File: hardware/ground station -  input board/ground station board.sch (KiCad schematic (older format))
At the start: 28 parts, among them J1 Conn_01x08_Female, J10 High_Pwr_Connector(Female), J2 Conn_01x08_Male, J3 Conn_01x08_Female, J4 Conn_01x08_Male, J5 Conn_01x06_Female, J6 Conn_01x06_Male, J7 Conn_01x06_Female, J8 Conn_01x06_Male, J9 Battery_Connector(Male)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

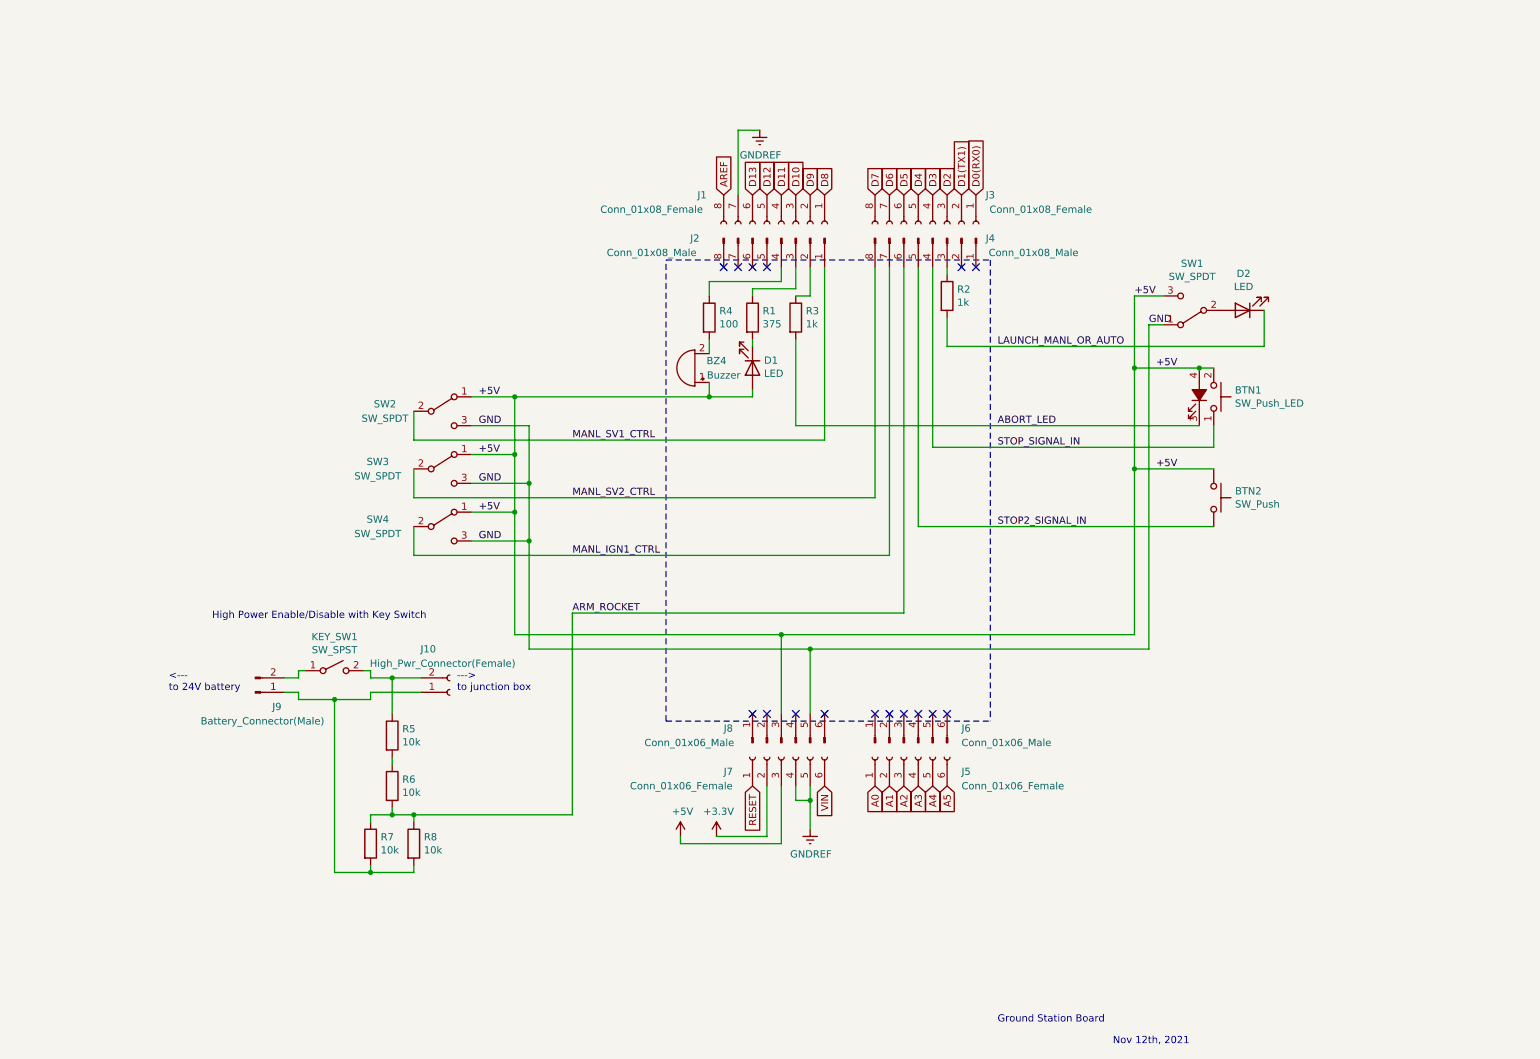
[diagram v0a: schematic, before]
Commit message: Updated Ground Station board, Junction Box sensor board, and Junction Box high power board.
Moved Ground Station pins so that abort (STOP), backup abort (BACKUP_STOP),  auto/manual launch (LAUNCH_MANL_OR_AUTO), and arming (ARM_ROCKET) signals now each go to an Arduino pin that can handle external interrupts. Shifted the rest of the pins so that the manual control pins for SV1, SV2, and IGN1 all connect to the same header on the Arduino. Added battery and outlet for extension cord to key switch circuit. Removed some male header pins because red radio XBee board must connect to them on Arduino instead. As  a consequence, the armed status buzzer/LED pins connect to male headers a level below the board using wires. XBee board also blocks nearest 5V/GND pins, so power must be obtained from the very end of the
Arduino Mega board, using external wires connected to male headers.

Added fuses to high power board. One fuse for each solid state relay, and one fuse from the main 24V high power line.

Corrected wiring for GND, D9, and D8 on sensor board's 4 pin connector (which controls the high power board). Also added a header symbol for the SDA/SCL lines, to indicate that the connections must jump a to a lower board level, down to the Arduino headers, using wires.
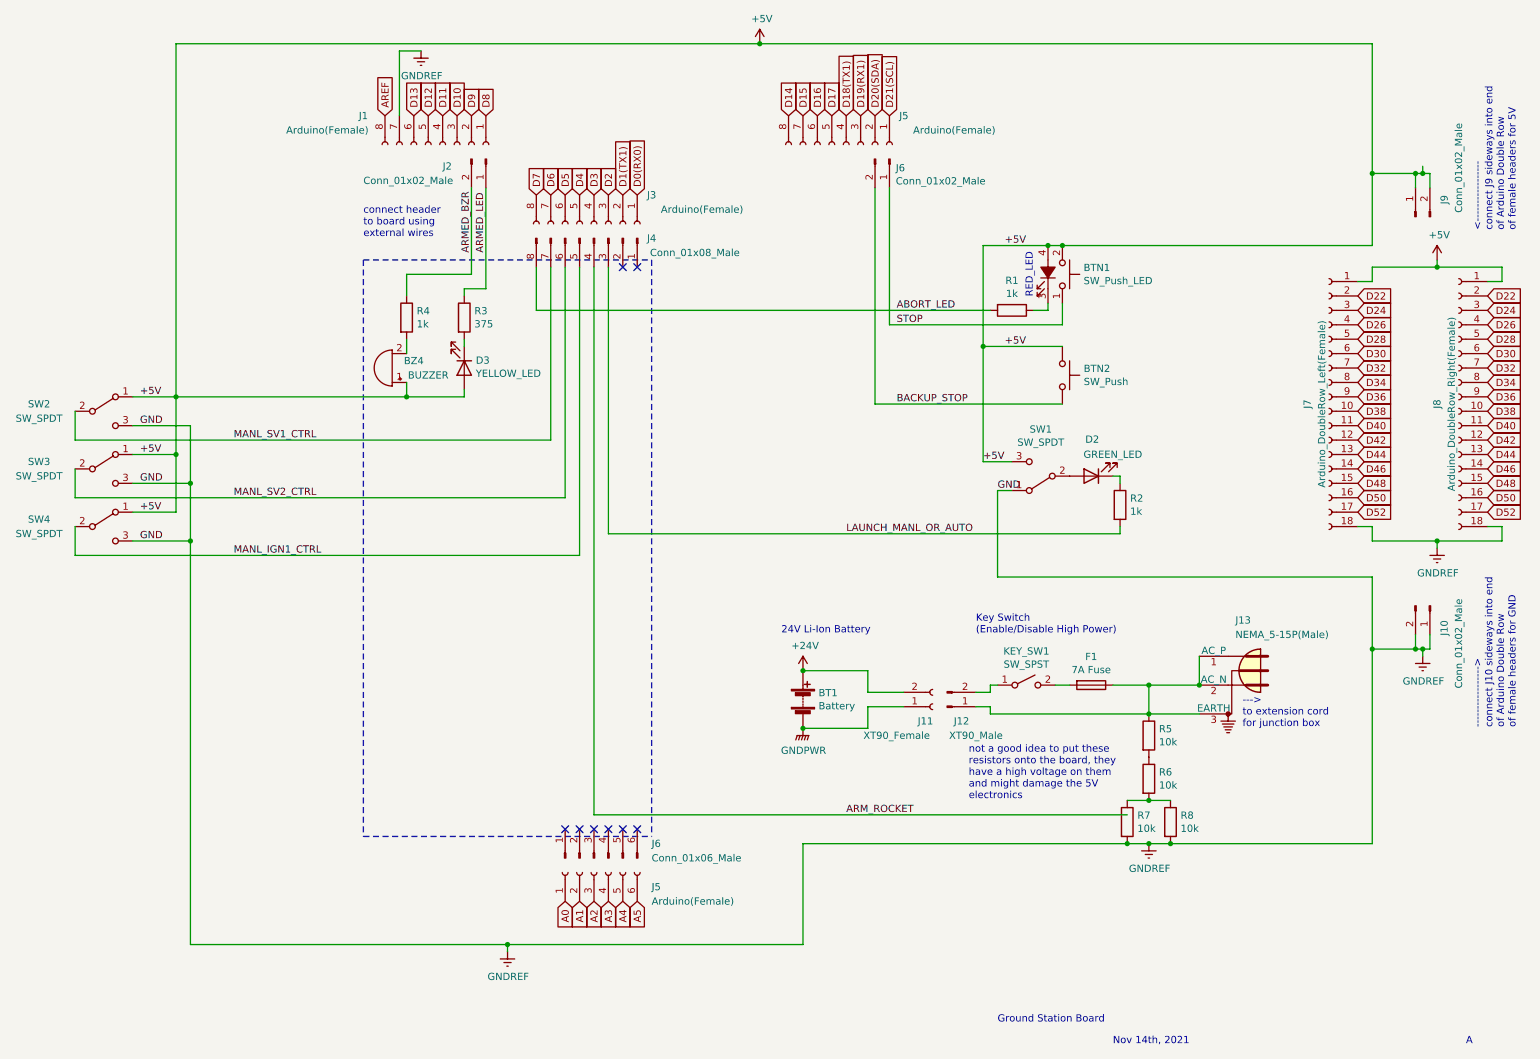
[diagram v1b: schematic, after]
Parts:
- removed J10: High_Pwr_Connector(Female), symbol Connector:Conn_01x02_Female
- removed J2: Conn_01x08_Male, symbol Connector:Conn_01x08_Male
- removed J7: Conn_01x06_Female, symbol Connector:Conn_01x06_Female
- removed J8: Conn_01x06_Male, symbol Connector:Conn_01x06_Male
- removed R3: 1k, symbol Device:R
- added BT1: Battery, symbol Device:Battery
- added F1: 7A Fuse, symbol Device:Fuse
- added J10, J2, J6, J9: Conn_01x02_Male, symbol Connector:Conn_01x02_Male
- added J11: XT90_Female, symbol Connector:Conn_01x02_Female
- added J13: NEMA_5-15P(Male), symbol Connector:Conn_WallPlug_Earth
- added J5: Arduino(Female), symbol Connector:Conn_01x08_Female
- added J7: Arduino_DoubleRow_Left(Female), symbol Connector:Conn_01x18_Female
- added J8: Arduino_DoubleRow_Right(Female), symbol Connector:Conn_01x18_Female
- added R1: 1k, symbol Device:R
- BZ4: value Buzzer -> BUZZER
- D2: value LED -> GREEN_LED
- D3: renamed from D1; value LED -> YELLOW_LED
- J1, J3: value Conn_01x08_Female -> Arduino(Female)
- J12: renamed from J9; value Battery_Connector(Male) -> XT90_Male
- J5: value Conn_01x06_Female -> Arduino(Female)
- R4: value 100 -> 1k
- renumbered R1 to R3
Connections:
- net GND is gone; now on net GNDREF: SW1.1 (A), SW2.3 (C), SW3.3 (C), SW4.3 (C)
- net +5V: now also J7.1 (Pin_1), J8.1 (Pin_1), J9.1 (Pin_1), J9.2 (Pin_2)
- net ABORT_LED: now also J4.8 (Pin_8), R1.2; no longer BTN1.3 (K)
- net ARM_ROCKET: now also J4.4 (Pin_4); no longer J4.6 (Pin_6), R6.2, R7.1, R8.1
- net GNDREF: now also R7.2, R8.2, J10.1 (Pin_1), J10.2 (Pin_2), J7.18 (Pin_18), J8.18 (Pin_18)
- net LAUNCH_MANL_OR_AUTO: now also J4.3 (Pin_3); no longer D2.1 (K)
- net MANL_IGN1_CTRL: now also J4.5 (Pin_5); no longer J4.7 (Pin_7)
- net MANL_SV1_CTRL: now also J4.7 (Pin_7)
- net MANL_SV2_CTRL: now also J4.6 (Pin_6); no longer J4.8 (Pin_8)
- net ARMED_LED: now reaches R3.1
- net ARMED_LED: now also J2.1 (Pin_1)
- net ARMED_BZR: now reaches R4.1
- net ARMED_BZR: now also J2.2 (Pin_2)
- net at R2.1: now also D2.1 (K); no longer J4.3 (Pin_3)
- net at KEY_SW1.2 (B): now also F1.2; no longer R5.1
- net STOP2_SIGNAL_IN renamed BACKUP_STOP
- net BACKUP_STOP: now also J6.2 (Pin_2); no longer J4.5 (Pin_5)
- net STOP_SIGNAL_IN renamed STOP
- net STOP: now also J6.1 (Pin_1); no longer J4.4 (Pin_4)
- new net: BTN1.3 (K), R1.1
- new net: F1.1, J12.1 (Pin_1), J13.1 (AC_P), J13.2 (AC_N), J13.3 (EARTH), R5.1
- new net: R6.2, R7.1, R8.1
- new net +24V: BT1.1 (+), J11.2 (Pin_2)
- new net D14: J5.8 (Pin_8)
- new net D15: J5.7 (Pin_7)
- new net D16: J5.6 (Pin_6)
- new net D17: J5.5 (Pin_5)
- new net D18(TX1): J5.4 (Pin_4)
- new net D19(RX1): J5.3 (Pin_3)
- new net D20(SDA): J5.2 (Pin_2)
- new net D21(SCL): J5.1 (Pin_1)
- new net D22: J7.2 (Pin_2), J8.2 (Pin_2)
- new net D24: J7.3 (Pin_3), J8.3 (Pin_3)
- new net D26: J7.4 (Pin_4), J8.4 (Pin_4)
- new net D28: J7.5 (Pin_5), J8.5 (Pin_5)
- new net D30: J7.6 (Pin_6), J8.6 (Pin_6)
- new net D32: J7.7 (Pin_7), J8.7 (Pin_7)
- new net D34: J7.8 (Pin_8), J8.8 (Pin_8)
- new net D36: J7.9 (Pin_9), J8.9 (Pin_9)
- new net D38: J7.10 (Pin_10), J8.10 (Pin_10)
- new net D40: J7.11 (Pin_11), J8.11 (Pin_11)
- new net D42: J7.12 (Pin_12), J8.12 (Pin_12)
- new net D44: J7.13 (Pin_13), J8.13 (Pin_13)
- new net D46: J7.14 (Pin_14), J8.14 (Pin_14)
- new net D48: J7.15 (Pin_15), J8.15 (Pin_15)
- new net D50: J7.16 (Pin_16), J8.16 (Pin_16)
- new net D52: J7.17 (Pin_17), J8.17 (Pin_17)
- new net GNDPWR: BT1.2 (-), J11.1 (Pin_1)
- no-connect marks 16 -> 8
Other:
- note added: "----------------->\nconnect J10 sideways into end \nof Arduino Double Row\nof female headers for GND"
- note added: "--->\nto extension cord \nfor junction box"
- note added: "24V Li-Ion Battery"
- note added: "<-----------------\nconnect J9 sideways into end \nof Arduino Double Row\nof female headers for 5V"
- note added: "A"
- note added: "Key Switch\n(Enable/Disable High Power)"
- note added: "Nov 14th, 2021"
- note added: "RED_LED"
- note added: "connect header\nto board using\nexternal wires"
- note added: "not a good idea to put these\nresistors onto the board, they\nhave a high voltage on them\nand might damage the 5V\nelectronics"
- note removed: "--->\nto junction box"
- note removed: "<---\nto 24V battery"
- note removed: "High Power Enable/Disable with Key Switch"
- note removed: "Nov 12th, 2021"
- moved on the sheet: BTN1, BTN2, BZ4, D2, D3, J1, J12, J3, J4, J5, J6, KEY_SW1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
